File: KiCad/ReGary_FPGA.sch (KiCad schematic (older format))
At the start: 29 parts, among them J1 Conn_01x02, U1 GW1N-UV1P5LQ100, U2 LM1117-3.3, U3 TPS73643DBV

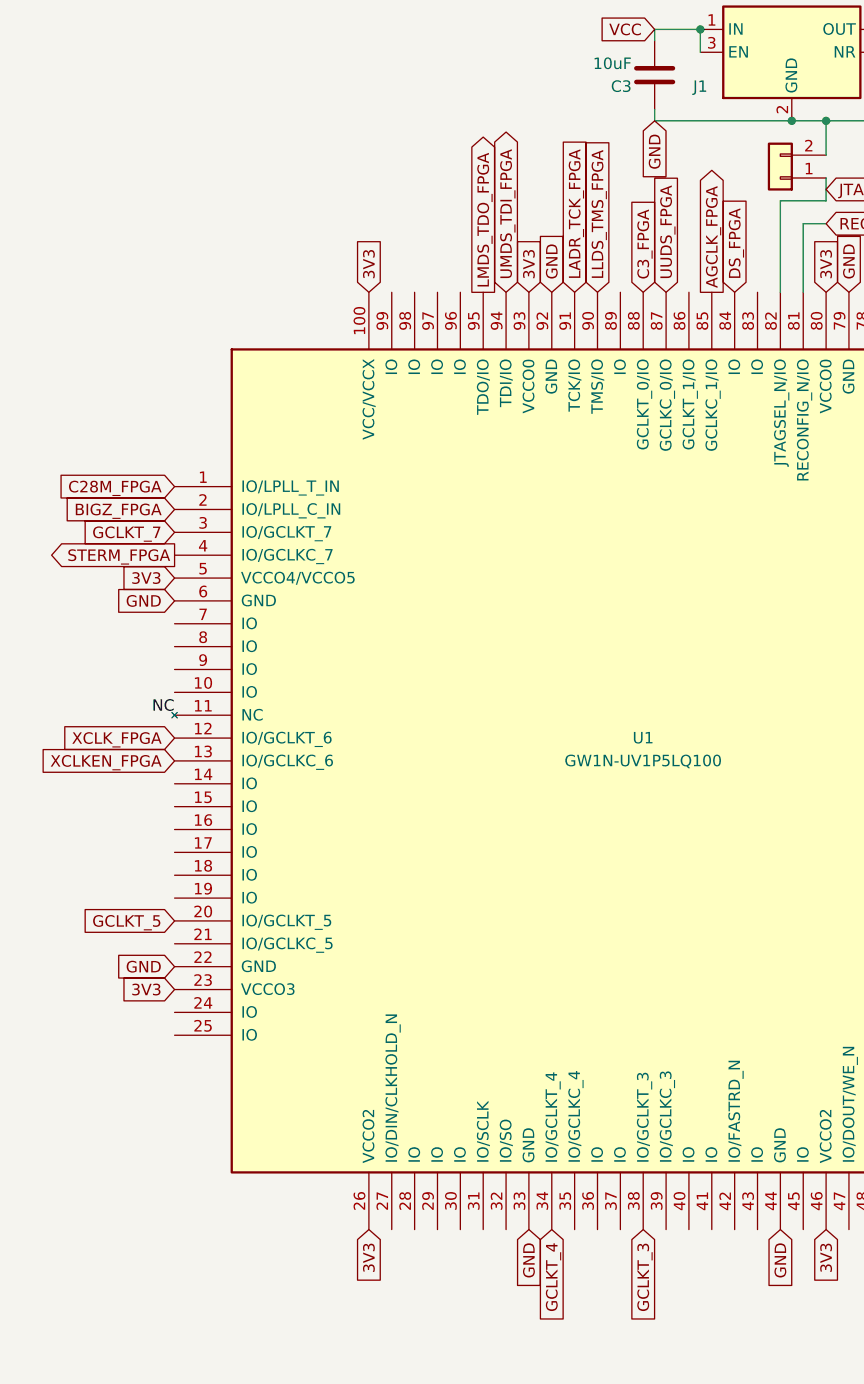
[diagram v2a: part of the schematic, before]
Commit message: More FPGA pin assignments and routing
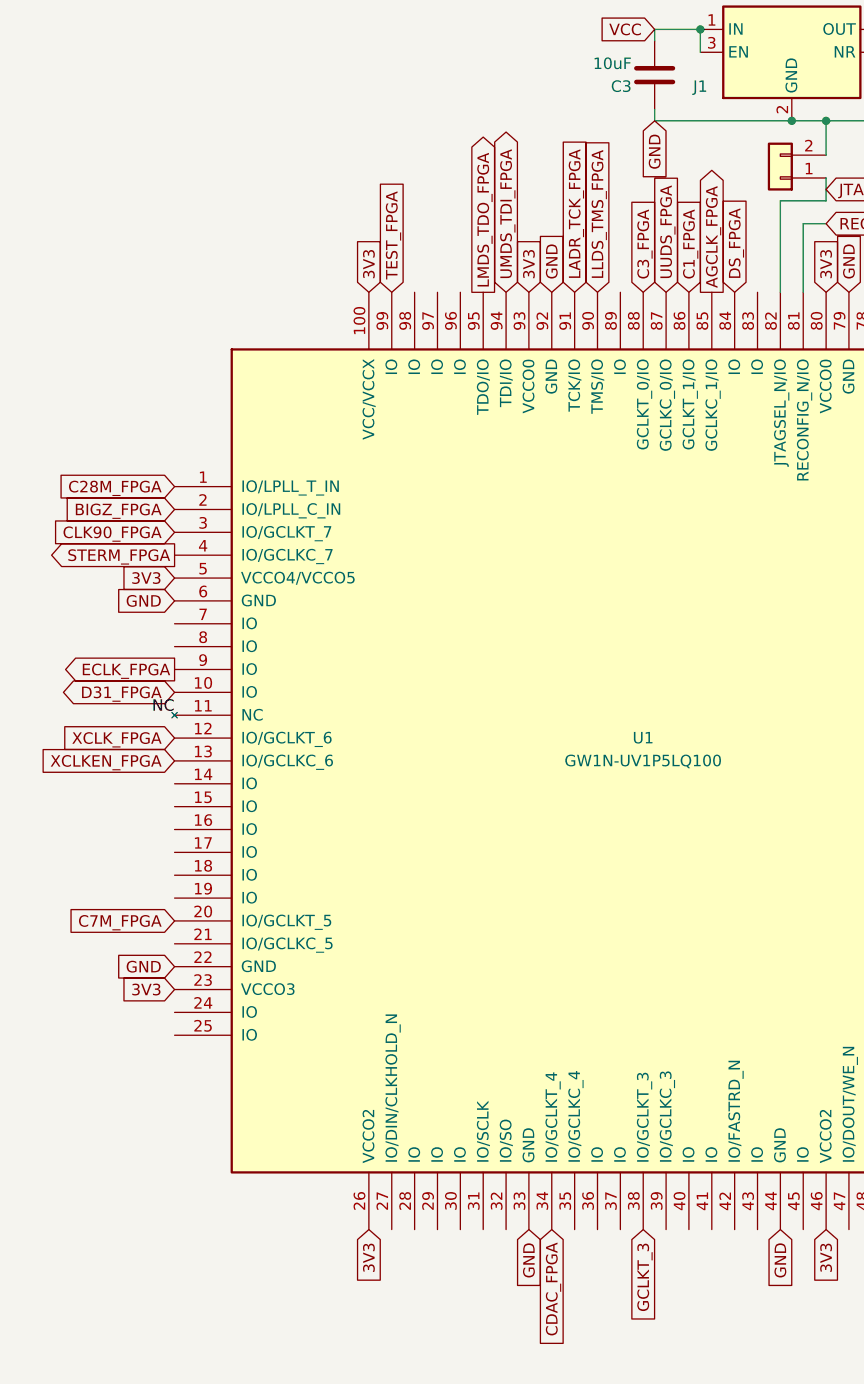
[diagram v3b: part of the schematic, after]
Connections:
- net labels added: C1_FPGA, C7M_FPGA, CDAC_FPGA, CLK90_FPGA, D31_FPGA, ECLK_FPGA, TEST_FPGA
- net labels removed: GCLKT_4, GCLKT_5, GCLKT_7
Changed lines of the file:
@@
 Text GLabel 3400 6200 3    50   Input ~ 0
 GCLKT_3
-Text GLabel 3000 6200 3    50   Input ~ 0
-GCLKT_4
-Text GLabel 1350 4850 0    50   Input ~ 0
-GCLKT_5
-Text GLabel 1350 3150 0    50   Input ~ 0
-GCLKT_7
 Text GLabel 1350 4150 0    50   Input ~ 0
 XCLKEN_FPGA
@@
 Text GLabel 1350 3050 0    50   Input ~ 0
 BIGZ_FPGA
+Text GLabel 1350 3850 0    50   BiDi ~ 0
+D31_FPGA
+Text GLabel 1350 3150 0    50   Input ~ 0
+CLK90_FPGA
+Text GLabel 2300 2100 1    50   Input ~ 0
+TEST_FPGA
+Text GLabel 1350 4850 0    50   Input ~ 0
+C7M_FPGA
+Text GLabel 3000 6200 3    50   Input ~ 0
+CDAC_FPGA
+Text GLabel 3600 2100 1    50   Input ~ 0
+C1_FPGA
+Text GLabel 1350 3750 0    50   Output ~ 0
+ECLK_FPGA
 $EndSCHEMATC

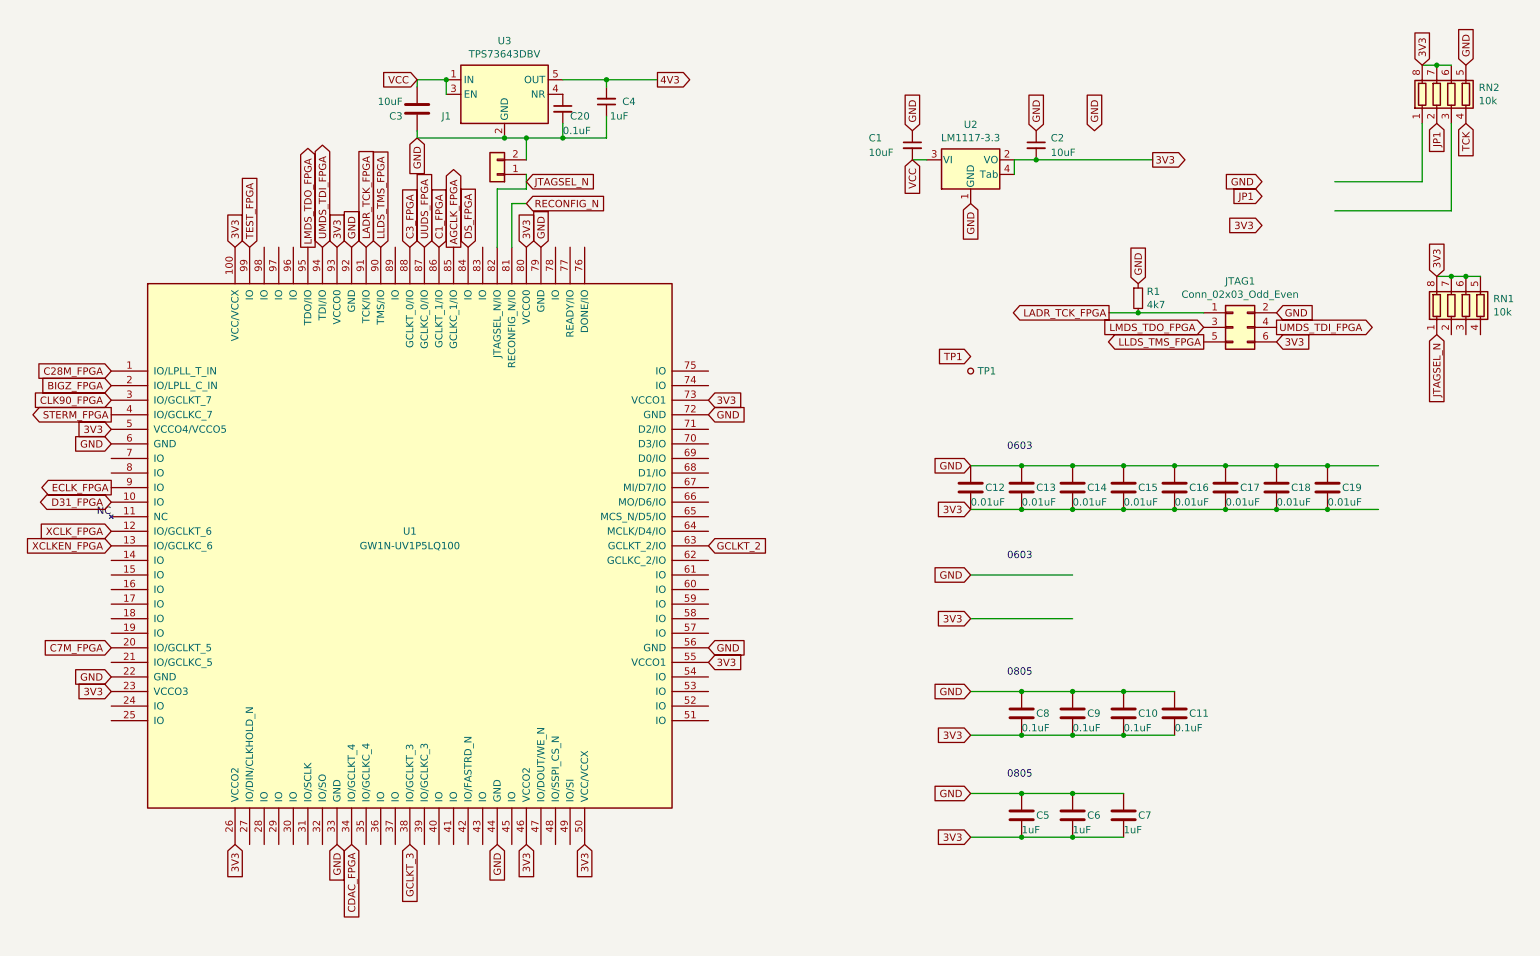
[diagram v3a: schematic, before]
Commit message: More signal to pin assignments and routing
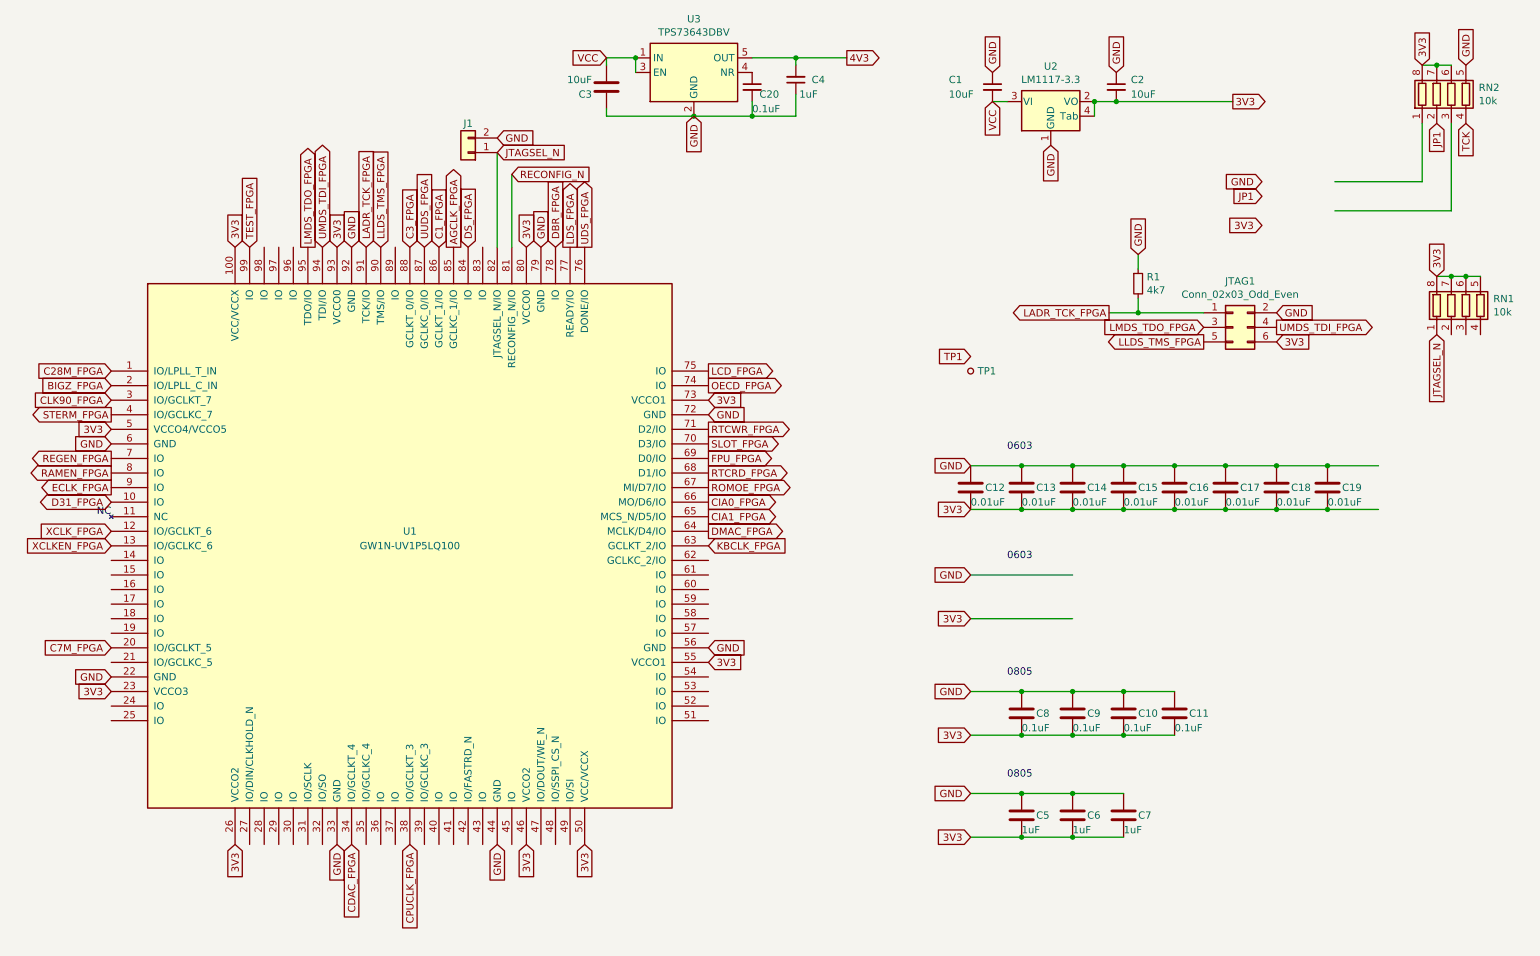
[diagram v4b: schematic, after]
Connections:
- net labels added: CIA0_FPGA, CIA1_FPGA, CPUCLK_FPGA, DBR_FPGA, DMAC_FPGA, FPU_FPGA, KBCLK_FPGA, LCD_FPGA, LDS_FPGA, OECD_FPGA, RAMEN_FPGA, REGEN_FPGA, ROMOE_FPGA, RTCRD_FPGA, RTCWR_FPGA, SLOT_FPGA, UDS_FPGA
- net labels removed: GCLKT_2, GCLKT_3
- wire segments 66 -> 63
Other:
- moved on the sheet: C1, C2, C20, C3, C4, J1, R1, U2, U3

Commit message: Placement of caps and more routing
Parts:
- removed RN2: 10k, ReGary:RESCAF80P320X160X60-8N, symbol Device:R_Pack04
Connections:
- net labels removed: TCK
- wire segments 63 -> 70
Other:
- moved on the sheet: RN1
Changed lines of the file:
@@
 Text GLabel 8400 2150 1    50   Input ~ 0
 GND
-Text GLabel 10350 850  1    50   Input ~ 0
-3V3
-Wire Wire Line
-	9750 1650 10350 1650
 Text GLabel 7250 3600 0    50   Input ~ 0
 GND
@@
 Connection ~ 9350 3900
 $Comp
-L Device:R_Pack04 RN2
-U 1 1 607B916D
-P 10550 1050
-F 0 "RN2" H 10738 1096 50  0000 L CNN
-F 1 "10k" H 10738 1005 50  0000 L CNN
-F 2 "ReGary:RESCAF80P320X160X60-8N" V 10825 1050 50  0001 C CNN
-F 3 "~" H 10550 1050 50  0001 C CNN
-	1    10550 1050
-	1    0    0    -1
-$EndComp
-$Comp
 L Device:R_Pack04 RN1
 U 1 1 607E0507
-P 10650 2500
-F 0 "RN1" H 10838 2546 50  0000 L CNN
-F 1 "10k" H 10838 2455 50  0000 L CNN
-F 2 "ReGary:RESCAF80P320X160X60-8N" V 10925 2500 50  0001 C CNN
-F 3 "~" H 10650 2500 50  0001 C CNN
-	1    10650 2500
-	1    0    0    -1
-$EndComp
-Text GLabel 10450 2300 1    50   Input ~ 0
-3V3
-Wire Wire Line
-	10450 2300 10550 2300
-Wire Wire Line
-	9750 1850 10550 1850
-Wire Wire Line
-	10350 1250 10350 1650
-Text GLabel 10650 850  1    50   Input ~ 0
-GND
-Text GLabel 10650 1250 3    50   Input ~ 0
-TCK
+P 5800 1800
+F 0 "RN1" H 5988 1846 50  0000 L CNN
+F 1 "10k" H 5988 1755 50  0000 L CNN
+F 2 "ReGary:RESCAF80P320X160X60-8N" V 6075 1800 50  0001 C CNN
+F 3 "~" H 5800 1800 50  0001 C CNN
+	1    5800 1800
+	1    0    0    -1
+$EndComp
+Text GLabel 5600 1600 1    50   Input ~ 0
+3V3
+Wire Wire Line
+	5600 1600 5700 1600
 $Comp
 L Device:C C?
@@
 Text GLabel 9250 1750 0    50   Input ~ 0
 JP1
-Text GLabel 10450 1250 3    50   Input ~ 0
-JP1
-Wire Wire Line
-	10350 850  10450 850
 $Comp
 L Device:C C?
@@
 TP1
 Wire Wire Line
-	10550 2300 10650 2300
-Connection ~ 10550 2300
+	5700 1600 5800 1600
+Connection ~ 5700 1600
 $Comp
 L Connector:TestPoint_Small TP1
@@
 $EndComp
 Wire Wire Line
-	10650 2300 10750 2300
-Connection ~ 10650 2300
-Wire Wire Line
-	10450 850  10550 850
-Connection ~ 10450 850
-Wire Wire Line
-	10550 1250 10550 1850
+	5800 1600 5900 1600
+Connection ~ 5800 1600
 $Comp
 L Device:C_Small C?
@@
 Text GLabel 4000 1450 2    50   Input ~ 0
 JTAGSEL_N
-Text GLabel 10450 2700 3    50   Input ~ 0
+Text GLabel 5600 2000 3    50   Input ~ 0
 JTAGSEL_N
 $Comp
@@
 Text GLabel 4400 2100 1    50   Input ~ 0
 DBR_FPGA
-Text GLabel 4500 2100 1    50   Output ~ 0
+Text GLabel 4850 1900 1    50   Output ~ 0
 LDS_FPGA
-Text GLabel 4600 2100 1    50   Output ~ 0
+Text GLabel 5050 1900 1    50   Output ~ 0
 UDS_FPGA
+Text GLabel 5700 2000 3    50   Input ~ 0
+RECONFIG_N
+Wire Wire Line
+	5300 2750 5900 2750
+Wire Wire Line
+	5900 2750 5900 2000
+Wire Wire Line
+	5400 2650 5800 2650
+Wire Wire Line
+	5800 2650 5800 2000
+Wire Wire Line
+	5300 2750 5300 2100
+Wire Wire Line
+	5300 2100 5050 2100
+Wire Wire Line
+	4500 2100 4500 2000
+Wire Wire Line
+	4500 2000 4850 2000
+Wire Wire Line
+	5400 2000 5400 2650
+Connection ~ 4850 2000
+Wire Wire Line
+	4850 2000 5400 2000
+Connection ~ 5050 2100
+Wire Wire Line
+	5050 2100 4600 2100
+Wire Wire Line
+	4850 1900 4850 2000
+Wire Wire Line
+	5050 1900 5050 2100
 $EndSCHEMATC

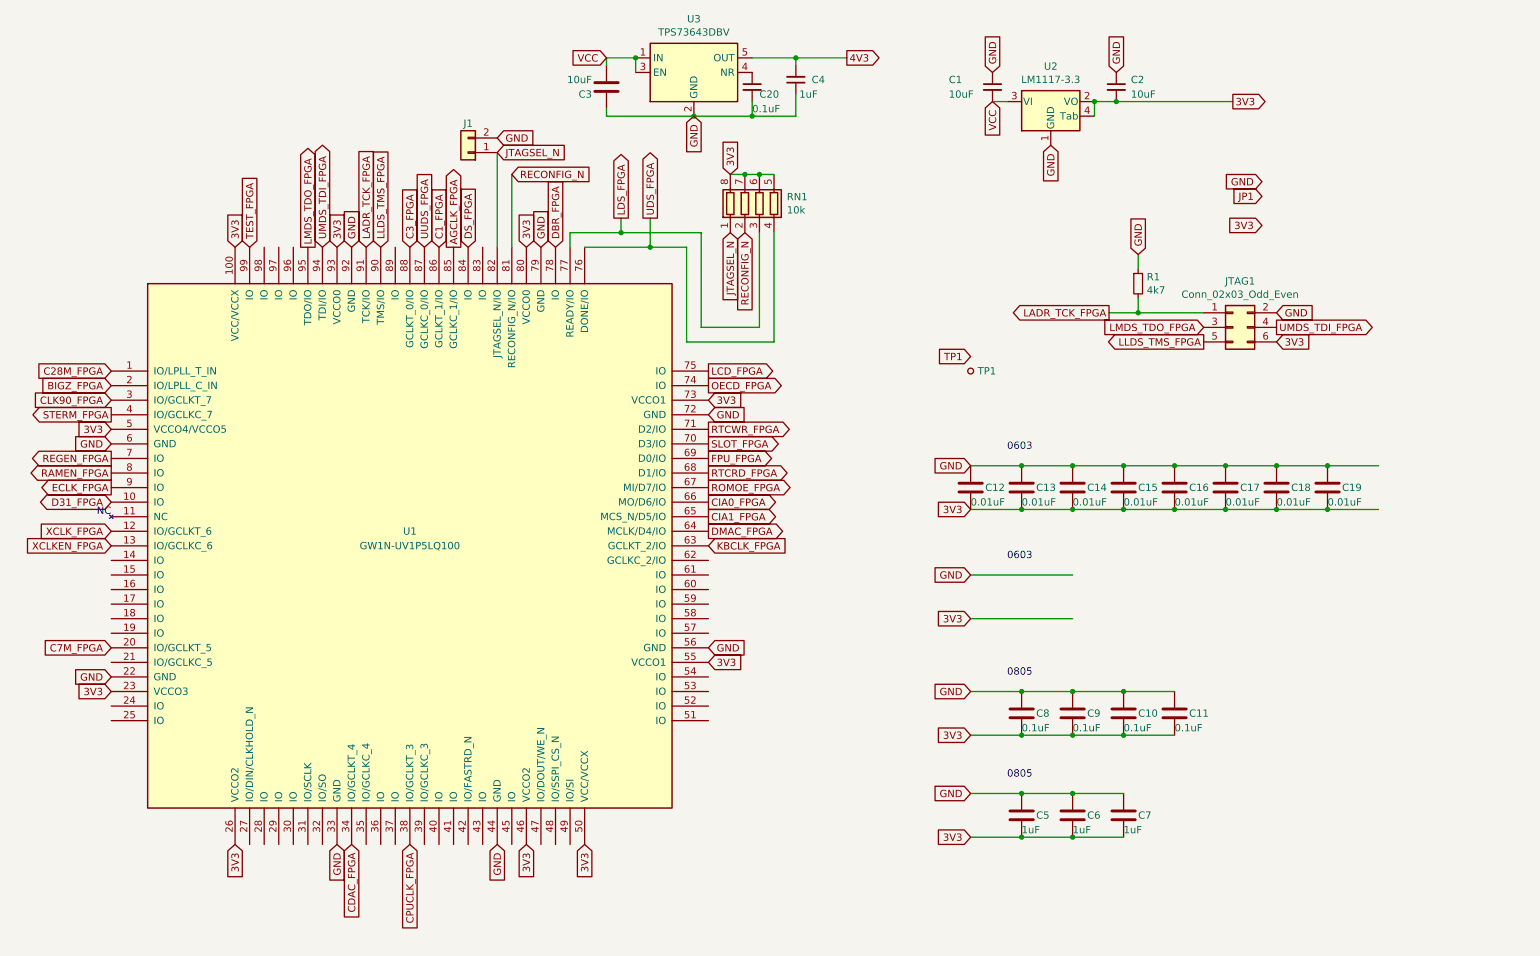
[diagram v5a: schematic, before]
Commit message: More signal to pin assignments and routing done, moved /REGEN and /RAMEN signals to FPGA pin 97,98
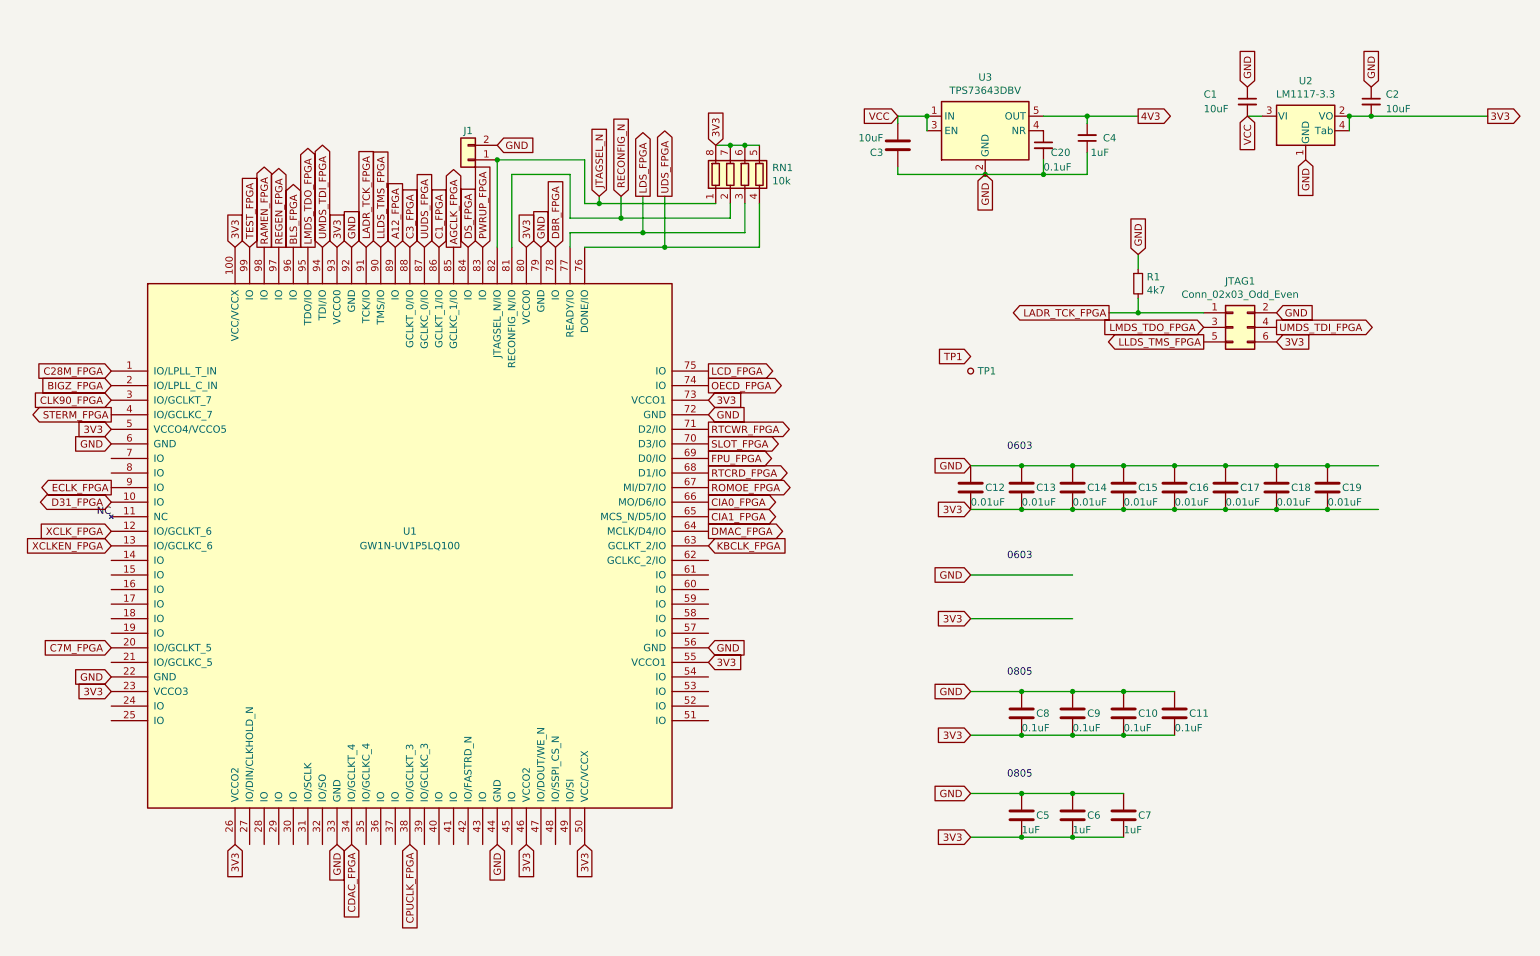
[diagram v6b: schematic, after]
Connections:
- net labels added: A12_FPGA, BLS_FPGA, PWRUP_FPGA
- net labels removed: JP1
- wire segments 70 -> 77
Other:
- moved on the sheet: C1, C2, C20, C3, C4, J1, RN1, U2, U3
